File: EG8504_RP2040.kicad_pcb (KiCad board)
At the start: 2 copper layers, 78 x 65 mm, 23 parts, among them J1 DM1B-DSF-PEJ, J2 522712079, J3 Conn_01x02_Socket, J4 Conn_01x08_Socket, SW2 SW_Push, U5 MC34063AD

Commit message: シルクの修正
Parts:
- moved REF** 4.12 mm to (62.0, 131.0)
- moved REF** 4.00 mm to (62.0, 72.0)
- moved REF** 1.00 mm to (130.0, 131.0)
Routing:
- net /DAT0: track 36.1 -> 37.8 mm
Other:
- board size 78 x 65 mm -> 74 x 65 mm
- board text removed: "${REFERENCE}"
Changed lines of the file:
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@@
 		(tags "SOIC SO")
 		(property "Reference" "U5"
-			(at 3.872 3.556 0)
+			(at 3.748 3.302 0)
 			(layer "F.SilkS")
 			(effects
@@
 		(tags "connector JST XH vertical")
 		(property "Reference" "J3"
-			(at 1.25 -3.55 0)
+			(at -4.5 -1.5 0)
 			(layer "F.SilkS")
 			(effects
@@
 	(footprint "MountingHole:MountingHole_2.2mm_M2_DIN965_Pad"
 		(layer "F.Cu")
-		(at 58 130)
+		(at 62 131)
 		(descr "Mounting Hole 2.2mm, M2, generated by kicad-footprint-generator mountinghole.py")
 		(tags "mountinghole M2 DIN965")
@@
 			(at 0 -2.85 0)
 			(layer "F.SilkS")
+			(hide yes)
 			(effects
 				(font
@@
 		(tags "connector JST XH vertical")
 		(property "Reference" "J4"
-			(at 8.75 -3.55 0)
+			(at -5 -1.5 0)
 			(layer "F.SilkS")
 			(effects
@@
 		(tags "SD card ")
 		(property "Reference" "J1"
-			(at -14 -4 90)
+			(at -13.773 -3.282 90)
 			(unlocked yes)
 			(layer "F.SilkS")
@@
 		(tags "resistor handsolder")
 		(property "Reference" "R10"
-			(at -3.5125 0 0)
+			(at -3.2785 -0.127 0)
 			(layer "F.SilkS")
 			(effects
@@
 	(footprint "MountingHole:MountingHole_2.2mm_M2_DIN965_Pad"
 		(layer "F.Cu")
-		(at 58 72)
+		(at 62 72)
 		(descr "Mounting Hole 2.2mm, M2, generated by kicad-footprint-generator mountinghole.py")
 		(tags "mountinghole M2 DIN965")
 		(property "Reference" "REF**"
-			(at 0 -2.85 0)
+			(at 4.992 -1.388 0)
 			(layer "F.SilkS")
+			(hide yes)
 			(effects
 				(font
@@
 		(tags "capacitor handsolder")
 		(property "Reference" "C18"
-			(at -3.5375 0 90)
+			(at -3.3285 0.889 90)
 			(layer "F.SilkS")
 			(effects
@@
 		(tags "inductor taiyo-yuden nr smd")
 		(property "Reference" "L1"
-			(at 0 -6.25 0)
+			(at 7.979 -0.927 180)
 			(layer "F.SilkS")
 			(effects
@@
 		(tags "resistor handsolder")
 		(property "Reference" "R9"
-			(at 3.1125 0 0)
+			(at 2.7705 0.127 0)
 			(layer "F.SilkS")
 			(effects
@@
 		(tags "522712079 ")
 		(property "Reference" "J2"
-			(at 0 -7.62 270)
+			(at 15.182018 -2.317982 0)
 			(unlocked yes)
 			(layer "F.SilkS")
@@
 		)
 		(property "Value" "522712079"
-			(at 0 -7.62 270)
+			(at -1.817982 1.682018 270)
 			(unlocked yes)
 			(layer "F.Fab")
+			(hide yes)
 			(effects
 				(font
@@
 			(layer "F.Fab")
 		)
-		(fp_text user "522712079"
-			(at 0 -10.16 270)
-			(unlocked yes)
-			(layer "F.SilkS")
-			(effects
-				(font
-					(size 1 1)
-					(thickness 0.15)
-				)
-			)
-		)
 		(fp_text user "${REFERENCE}"
-			(at 0 -7.62 270)
+			(at -12.817982 -5.317982 270)
 			(unlocked yes)
 			(layer "F.Fab")
@@
 		)
 		(fp_text user "522712079"
-			(at 0 -10.16 270)
+			(at 1.182018 5.682018 270)
 			(unlocked yes)
 			(layer "F.Fab")
@@
 		(tags "resistor handsolder")
 		(property "Reference" "R1"
-			(at 0 -1.43 0)
+			(at -1.1195 -1.524 0)
 			(layer "F.SilkS")
 			(effects
@@
 		(tags "resistor handsolder")
 		(property "Reference" "R2"
-			(at 0 -1.43 0)
+			(at 2.1825 1.524 0)
 			(layer "F.SilkS")
 			(effects
@@
 	(footprint "MountingHole:MountingHole_2.2mm_M2_DIN965_Pad"
 		(layer "F.Cu")
-		(at 130 130)
+		(at 130 131)
 		(descr "Mounting Hole 2.2mm, M2, generated by kicad-footprint-generator mountinghole.py")
 		(tags "mountinghole M2 DIN965")
@@
 			(at 0 -2.85 0)
 			(layer "F.SilkS")
+			(hide yes)
 			(effects
 				(font
@@
 		(tags "capacitor electrolytic")
 		(property "Reference" "C20"
-			(at 0 -6.3 90)
+			(at 6.902 -4.324 0)
 			(layer "F.SilkS")
 			(effects
@@
 		(tags "module usb pcb antenna")
 		(property "Reference" "A1"
-			(at 18.09 52.2175 270)
+			(at 18.034 51.054 90)
 			(unlocked yes)
 			(layer "F.SilkS")
@@
 		(tags "resistor handsolder")
 		(property "Reference" "R12"
-			(at 0 -1.43 0)
+			(at -3.3255 -0.127 0)
 			(layer "F.SilkS")
 			(effects
@@
 		(tags "resistor handsolder")
 		(property "Reference" "R11"
-			(at 0 -1.43 0)
+			(at -3.5795 -0.127 180)
 			(layer "F.SilkS")
 			(effects
@@
 		(tags "resistor handsolder")
 		(property "Reference" "R13"
-			(at -0.0875 1.8 90)
+			(at -3.2985 0.101 270)
 			(layer "F.SilkS")
 			(effects
@@
 	)
 	(gr_rect
-		(start 55.007034 69)
-		(end 132.992965 134)
+		(start 59 69)
+		(end 132.992966 134)
 		(stroke
 			(width 0.2)
@@
 		(layer "Edge.Cuts")
 	)
-	(gr_text "${REFERENCE}"
-		(at 68.326 96.774 270)
-		(layer "F.Fab")
-		(effects
-			(font
-				(size 1 1)
-				(thickness 0.15)
-			)
-		)
-	)
-	(gr_text "${REFERENCE}"
-		(at 74.168 89.916 90)
-		(layer "F.Fab")
-		(effects
-			(font
-				(size 1 1)
-				(thickness 0.15)
-			)
-		)
-	)
 	(segment
-		(start 102.129 77.237)
-		(end 101.6 77.237)
+		(start 116.84 89.408)
+		(end 116.84 88.9591)
 		(width 0.2)
 		(layer "F.Cu")
@@
 	)
 	(segment
-		(start 116.84 91.948)
-		(end 102.129 77.237)
+		(start 102.3515 77.216)
+		(end 101.621 77.216)
 		(width 0.2)
 		(layer "F.Cu")
@@
 	)
 	(segment
-		(start 102.3515 77.216)
-		(end 101.621 77.216)
+		(start 105.1179 77.237)
+		(end 101.6 77.237)
 		(width 0.2)
 		(layer "F.Cu")
@@
 		(net 1)
 	)
+	(segment
+		(start 116.84 88.9591)
+		(end 105.1179 77.237)
+		(width 0.2)
+		(layer "F.Cu")
+		(net 1)
+	)
 	(via
-		(at 116.84 91.948)
+		(at 116.84 89.408)
 		(size 0.6)
 		(drill 0.3)
@@
 	(segment
 		(start 116.84 105.918)
-		(end 116.84 91.948)
+		(end 116.84 89.408)
 		(width 0.2)
 		(layer "B.Cu")
@@
 	)
 	(segment
-		(start 103.004 82.162)
-		(end 101.6 82.162)
+		(start 117.729 94.615)
+		(end 105.283 82.169)
 		(width 0.2)
 		(layer "F.Cu")
@@
 	)
 	(segment
-		(start 105.283 82.169)
-		(end 103.011 82.169)
+		(start 103.004 82.162)
+		(end 101.6 82.162)
 		(width 0.2)
 		(layer "F.Cu")
@@
 	)
 	(segment
-		(start 121.92 98.806)
-		(end 105.283 82.169)
+		(start 103.011 82.169)
+		(end 103.004 82.162)
 		(width 0.2)
 		(layer "F.Cu")
@@
 	)
 	(segment
-		(start 103.011 82.169)
-		(end 103.004 82.162)
+		(start 105.283 82.169)
+		(end 103.011 82.169)
 		(width 0.2)
 		(layer "F.Cu")
@@
 	)
 	(via
-		(at 121.92 98.806)
+		(at 117.729 94.615)
 		(size 0.6)
 		(drill 0.3)
@@
 	)
 	(segment
+		(start 117.729 94.615)
+		(end 121.92 98.806)
+		(width 0.2)
+		(layer "B.Cu")
+		(net 9)
+	)
+	(segment
 		(start 81.279 80.517)
 		(end 83.185 82.423)
@@
 		(polygon
 			(pts
-				(xy 55 69) (xy 133 69) (xy 133 134) (xy 55 134)
+				(xy 59 69) (xy 133 69) (xy 133 134) (xy 59 134)
 			)
 		)

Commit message: 修正
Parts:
- moved J3 0.50 mm to (121.5, 130.0)
- moved J4 0.50 mm to (105.0, 130.0)
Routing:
- net /GPIO16: track 12.3 -> 11.8 mm
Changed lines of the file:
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@@
 	(footprint "Connector_JST:JST_XH_B2B-XH-A_1x02_P2.50mm_Vertical"
 		(layer "F.Cu")
-		(at 121.5 130.5 180)
+		(at 121.5 130 180)
 		(descr "JST XH series connector, B2B-XH-A (http://www.jst-mfg.com/product/pdf/eng/eXH.pdf), generated with kicad-footprint-generator")
 		(tags "connector JST XH vertical")
@@
 	(footprint "Connector_JST:JST_XH_B8B-XH-A_1x08_P2.50mm_Vertical"
 		(layer "F.Cu")
-		(at 105 130.5 180)
+		(at 105 130 180)
 		(descr "JST XH series connector, B8B-XH-A (http://www.jst-mfg.com/product/pdf/eng/eXH.pdf), generated with kicad-footprint-generator")
 		(tags "connector JST XH vertical")
@@
 	)
 	(segment
-		(start 112.578 130.5)
-		(end 119.38 123.698)
-		(width 0.4)
-		(layer "F.Cu")
-		(net 3)
-	)
-	(segment
 		(start 125.175 102.108)
 		(end 121.666 102.108)
@@
 	)
 	(segment
-		(start 105.5 130.5)
-		(end 112.578 130.5)
-		(width 0.4)
-		(layer "F.Cu")
-		(net 3)
-	)
-	(segment
 		(start 121.666 102.108)
 		(end 104.22 84.662)
@@
 	)
 	(segment
+		(start 113.078 130)
+		(end 119.38 123.698)
+		(width 0.4)
+		(layer "F.Cu")
+		(net 3)
+	)
+	(segment
 		(start 125.73 117.348)
 		(end 125.73 105.156)
@@
 		(net 3)
 	)
+	(segment
+		(start 105 130)
+		(end 113.078 130)
+		(width 0.4)
+		(layer "F.Cu")
+		(net 3)
+	)
 	(via
 		(at 68.664001 94.318001)
@@
 	(segment
 		(start 121.5 130.5)
-		(end 121.5 129.198)
+		(end 121.5 130)
 		(width 0.4)
 		(layer "F.Cu")
@@
 	)
 	(segment
-		(start 121.5 129.198)
-		(end 127 123.698)
+		(start 121.5 130)
+		(end 121.5 129.198)
 		(width 0.4)
 		(layer "F.Cu")
@@
 		(net 6)
 	)
+	(segment
+		(start 121.5 129.198)
+		(end 127 123.698)
+		(width 0.4)
+		(layer "F.Cu")
+		(net 6)
+	)
 	(via
 		(at 93.599 88.011)
@@
 	)
 	(segment
-		(start 84.582 127)
-		(end 87.884 127)
+		(start 86.942 127)
+		(end 90 130.058)
 		(width 0.4)
 		(layer "F.Cu")
@@
 	)
 	(segment
-		(start 87.884 127)
-		(end 90 129.116)
+		(start 90 130.058)
+		(end 90 130.5)
 		(width 0.4)
 		(layer "F.Cu")
@@
 	)
 	(segment
-		(start 90 129.116)
-		(end 90 130.5)
+		(start 84.582 127)
+		(end 86.942 127)
 		(width 0.4)
 		(layer "F.Cu")
@@
 	)
 	(segment
-		(start 85.09 126.238)
-		(end 83.82 124.968)
+		(start 92.5 130)
+		(end 88.738 126.238)
 		(width 0.4)
 		(layer "F.Cu")
@@
 	(segment
 		(start 92.5 130.5)
-		(end 88.238 126.238)
+		(end 92.5 130)
 		(width 0.4)
 		(layer "F.Cu")
@@
 	)
 	(segment
-		(start 88.238 126.238)
+		(start 83.82 124.968)
+		(end 83.82 123.698)
+		(width 0.4)
+		(layer "F.Cu")
+		(net 17)
+	)
+	(segment
+		(start 88.738 126.238)
 		(end 85.09 126.238)
 		(width 0.4)
@@
 	)
 	(segment
-		(start 83.82 124.968)
-		(end 83.82 123.698)
+		(start 85.09 126.238)
+		(end 83.82 124.968)
 		(width 0.4)
 		(layer "F.Cu")
@@
 	)
 	(segment
-		(start 102.5 130.5)
-		(end 109.22 123.78)
+		(start 102.5 130)
+		(end 108.802 123.698)
 		(width 0.4)
 		(layer "F.Cu")
@@
 	)
 	(segment
-		(start 109.22 123.78)
+		(start 108.802 123.698)
 		(end 109.22 123.698)
 		(width 0.4)
@@
 	)
 	(segment
-		(start 106.68 123.698)
-		(end 100 130.378)
+		(start 102.5 130.5)
+		(end 102.5 130)
 		(width 0.4)
 		(layer "F.Cu")
-		(net 48)
+		(net 47)
 	)
 	(segment
-		(start 100 130.378)
+		(start 100 130)
 		(end 100 130.5)
 		(width 0.4)
 		(layer "F.Cu")
+		(net 48)
+	)
+	(segment
+		(start 106.302 123.698)
+		(end 100 130)
+		(width 0.4)
+		(layer "F.Cu")
+		(net 48)
+	)
+	(segment
+		(start 106.68 123.698)
+		(end 106.302 123.698)
+		(width 0.4)
+		(layer "F.Cu")

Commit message: DHT11を追加
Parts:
- added J5: Conn_01x04_Socket, Connector_JST:JST_XH_B4B-XH-A_1x04_P2.50mm_Vertical, F.Cu at (67.8, 118.1)
- added JP1: SolderJumper_2_Open, Jumper:SolderJumper-2_P1.3mm_Open_RoundedPad1.0x1.5mm, F.Cu at (72.4, 123.7)
- added R3: 10k, Resistor_SMD:R_0603_1608Metric_Pad0.98x0.95mm_HandSolder, F.Cu at (72.6, 119.0)
- moved SW2 6.82 mm to (76.5, 129.0), turned to 90 degrees
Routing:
- net +3.3V: track 154.0 -> 191.0 mm
- net /GPIO15: track 0.00 -> 24.0 mm
- net Net-(J5-Pin_3): track 0.00 -> 4.70 mm
- net /D7: track 23.0 -> 24.1 mm
- net /RUN: track 34.2 -> 34.9 mm
- net GND: vias 0 -> 19

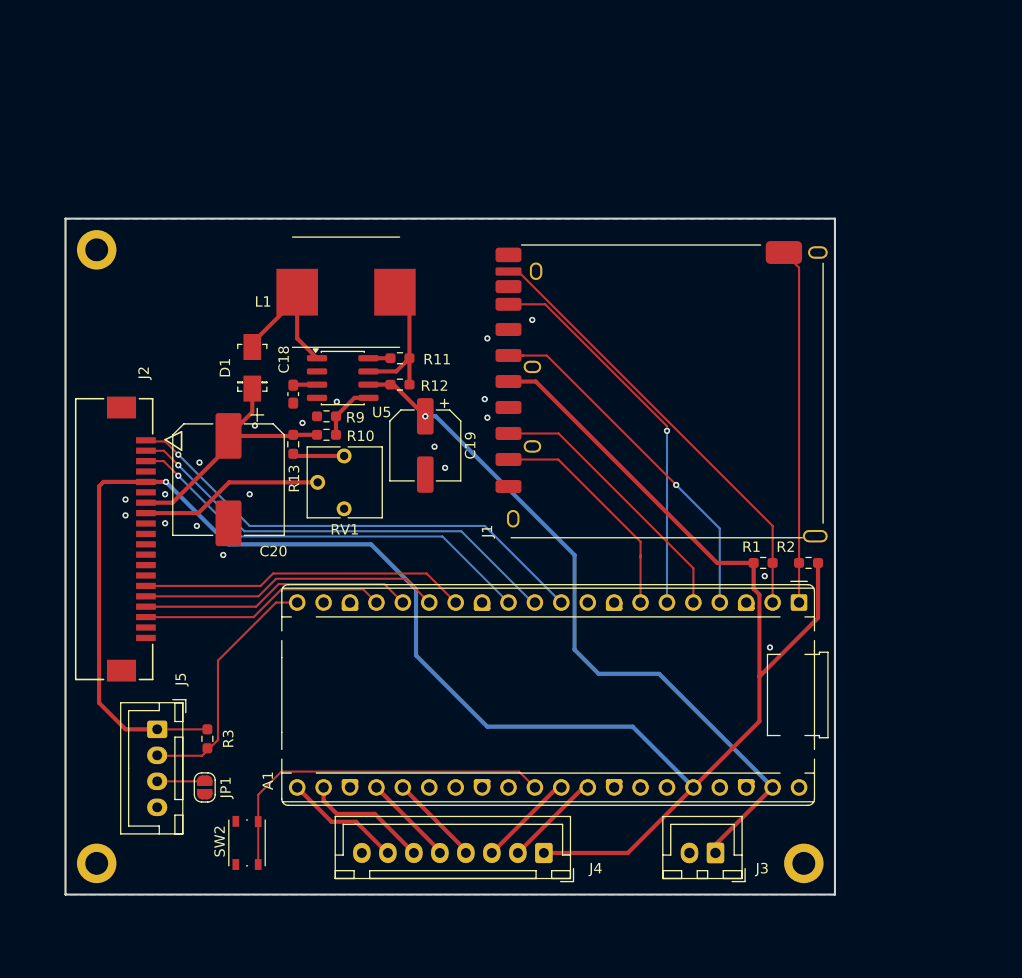
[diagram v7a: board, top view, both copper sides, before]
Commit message: スルーホール抵抗に
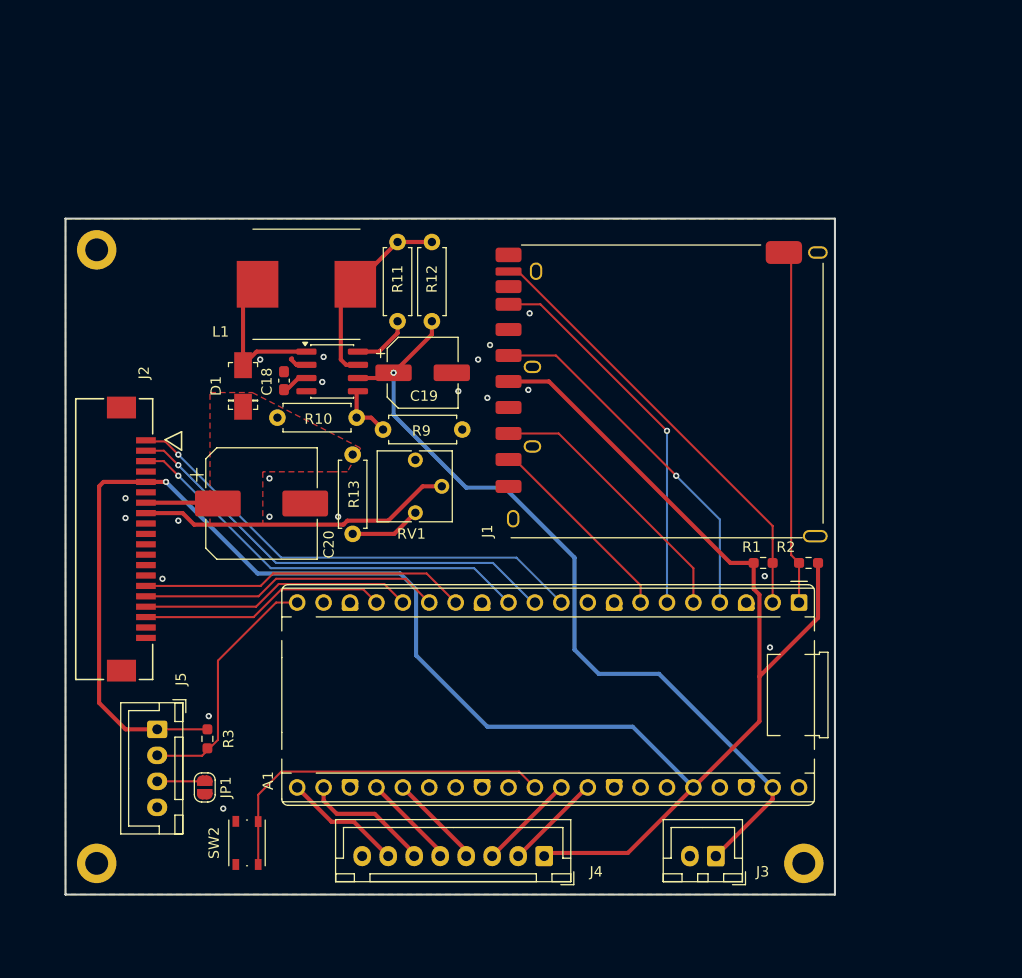
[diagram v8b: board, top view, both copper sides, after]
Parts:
- R10, R11, R12, R13, R9: footprint Resistor_SMD:R_0603_1608Metric_Pad0.98x0.95mm_HandSolder -> Resistor_THT:R_Axial_DIN0207_L6.3mm_D2.5mm_P7.62mm_Horizontal
- moved R12 14.1 mm to (94.2, 71.2), turned to -90 degrees
- moved R9 13.1 mm to (97.2, 89.3), turned to 180 degrees
- moved R11 11.2 mm to (90.9, 71.2), turned to -90 degrees
- moved R13 10.3 mm to (86.6, 99.3)
- moved RV1 8.76 mm to (92.6, 97.3), turned to 0 degrees
- moved C19 7.00 mm to (93.3, 83.8), turned to 0 degrees
- moved C20 3.92 mm to (77.8, 96.4), turned to 0 degrees
- moved L1 3.89 mm to (82.2, 75.3)
- moved R10 3.33 mm to (87.0, 88.1)
- moved D1 1.96 mm to (76.1, 85.1)
- moved C18 1.57 mm to (80.0, 84.6), turned to 90 degrees
- moved U5 1.20 mm to (84.6, 83.7)
- moved J3 0.30 mm to (121.5, 130.3)
- moved J4 0.30 mm to (105.0, 130.3)
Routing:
- net /VDOH: track 25.3 -> 6.95 mm
- net /VLCD: track 17.7 -> 30.4 mm
- net +5V: track 69.3 -> 80.1 mm
- net Net-(U5-Ipk): track 13.9 -> 18.7 mm
- net Net-(U5-DC): track 2.11 -> 5.69 mm
- net /CD/DAT3: track 22.2 -> 19.5 mm
- net Net-(R13-Pad1): track 4.98 -> 6.87 mm
- net GND: track 0.00 -> 1.85 mm, vias 19 -> 20
- net Net-(U5-SwC): track 14.2 -> 15.0 mm
- net /CLK: track 34.3 -> 34.8 mm
- added copper zone on F.Cu, net /VDOH
